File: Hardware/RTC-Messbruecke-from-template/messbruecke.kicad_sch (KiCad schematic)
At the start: 24 parts, among them U3 MAX6105, U4 LM324

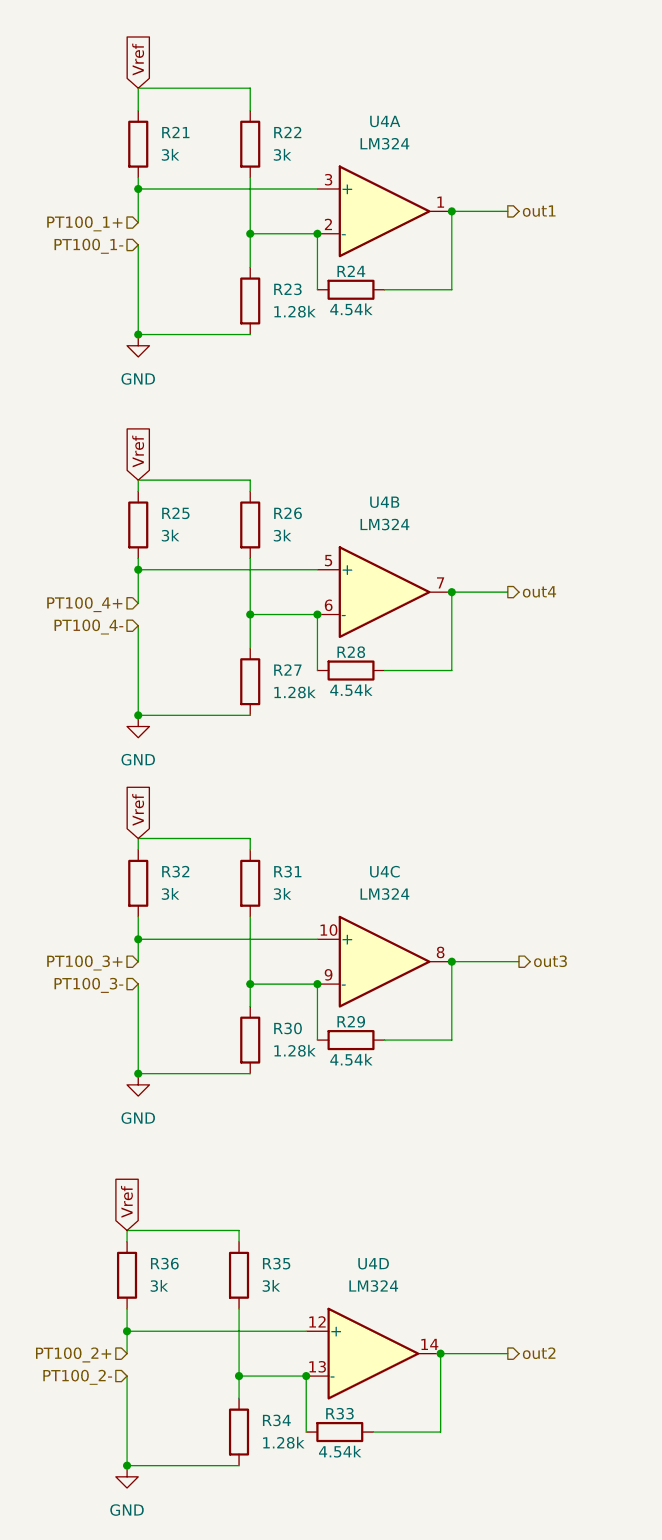
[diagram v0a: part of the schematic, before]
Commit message: added picture of schematic
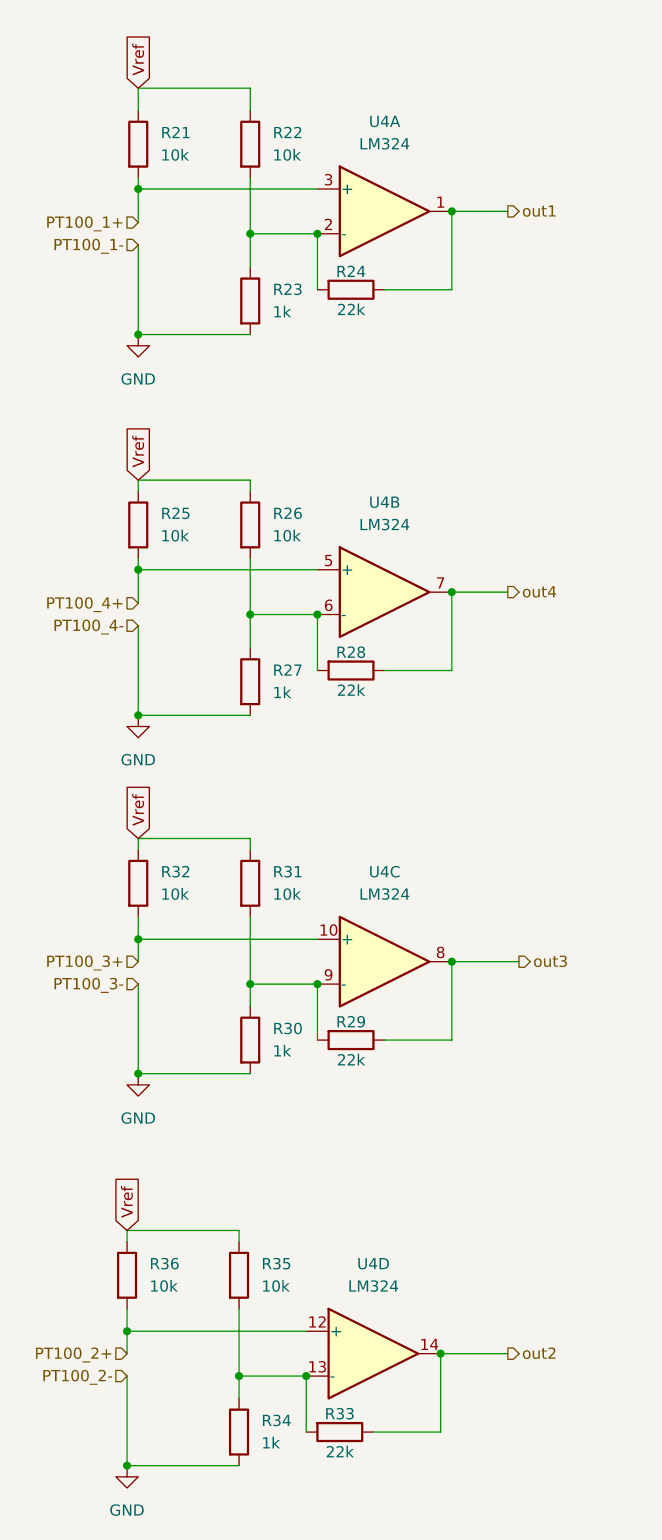
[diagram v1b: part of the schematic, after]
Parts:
- R21, R22, R25, R26, R31, R32, R35, R36: value 3k -> 10k
- R23, R27, R30, R34: value 1.28k -> 1k
- R24, R28, R29, R33: value 4.54k -> 22k
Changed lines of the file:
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@@
 			)
 		)
-		(property "Value" "3k"
+		(property "Value" "10k"
 			(at 50.8 161.2899 0)
 			(effects
@@
 			)
 		)
-		(property "Value" "1.28k"
+		(property "Value" "1k"
 			(at 52.07 134.6199 0)
 			(effects
@@
 			)
 		)
-		(property "Value" "1.28k"
+		(property "Value" "1k"
 			(at 52.07 50.7999 0)
 			(effects
@@
 			)
 		)
-		(property "Value" "4.54k"
+		(property "Value" "22k"
 			(at 59.69 180.086 90)
 			(effects
@@
 			)
 		)
-		(property "Value" "4.54k"
+		(property "Value" "22k"
 			(at 60.96 135.636 90)
 			(effects
@@
 			)
 		)
-		(property "Value" "3k"
+		(property "Value" "10k"
 			(at 38.1 161.2899 0)
 			(effects
@@
 			)
 		)
-		(property "Value" "1.28k"
+		(property "Value" "1k"
 			(at 50.8 179.0699 0)
 			(effects
@@
 			)
 		)
-		(property "Value" "3k"
+		(property "Value" "10k"
 			(at 52.07 33.0199 0)
 			(effects
@@
 			)
 		)
-		(property "Value" "3k"
+		(property "Value" "10k"
 			(at 39.37 33.0199 0)
 			(effects
@@
 			)
 		)
-		(property "Value" "1.28k"
+		(property "Value" "1k"
 			(at 52.07 93.9799 0)
 			(effects
@@
 			)
 		)
-		(property "Value" "3k"
+		(property "Value" "10k"
 			(at 52.07 116.8399 0)
 			(effects
@@
 			)
 		)
-		(property "Value" "4.54k"
+		(property "Value" "22k"
 			(at 60.96 93.726 90)
 			(effects
@@
 			)
 		)
-		(property "Value" "3k"
+		(property "Value" "10k"
 			(at 39.37 116.8399 0)
 			(effects
@@
 			)
 		)
-		(property "Value" "3k"
+		(property "Value" "10k"
 			(at 39.37 76.1999 0)
 			(effects
@@
 			)
 		)
-		(property "Value" "4.54k"
+		(property "Value" "22k"
 			(at 60.96 50.546 90)
 			(effects
@@
 			)
 		)
-		(property "Value" "3k"
+		(property "Value" "10k"
 			(at 52.07 76.1999 0)
 			(effects

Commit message: modified readme
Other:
- company: (none) -> LMWB
- title: Template Arduino Shield Simple Outline -> 4-Fach Messbruecke PT1000
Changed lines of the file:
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@@
 	(paper "A4")
 	(title_block
-		(title "Template Arduino Shield Simple Outline")
-		(date "2024-08-05")
+		(title "4-Fach Messbruecke PT1000")
+		(date "2024-09-02")
 		(rev "v.0.2")
+		(company "LMWB")
+		(comment 1 "Lukas Bartels 2024")
 	)
 	(junction

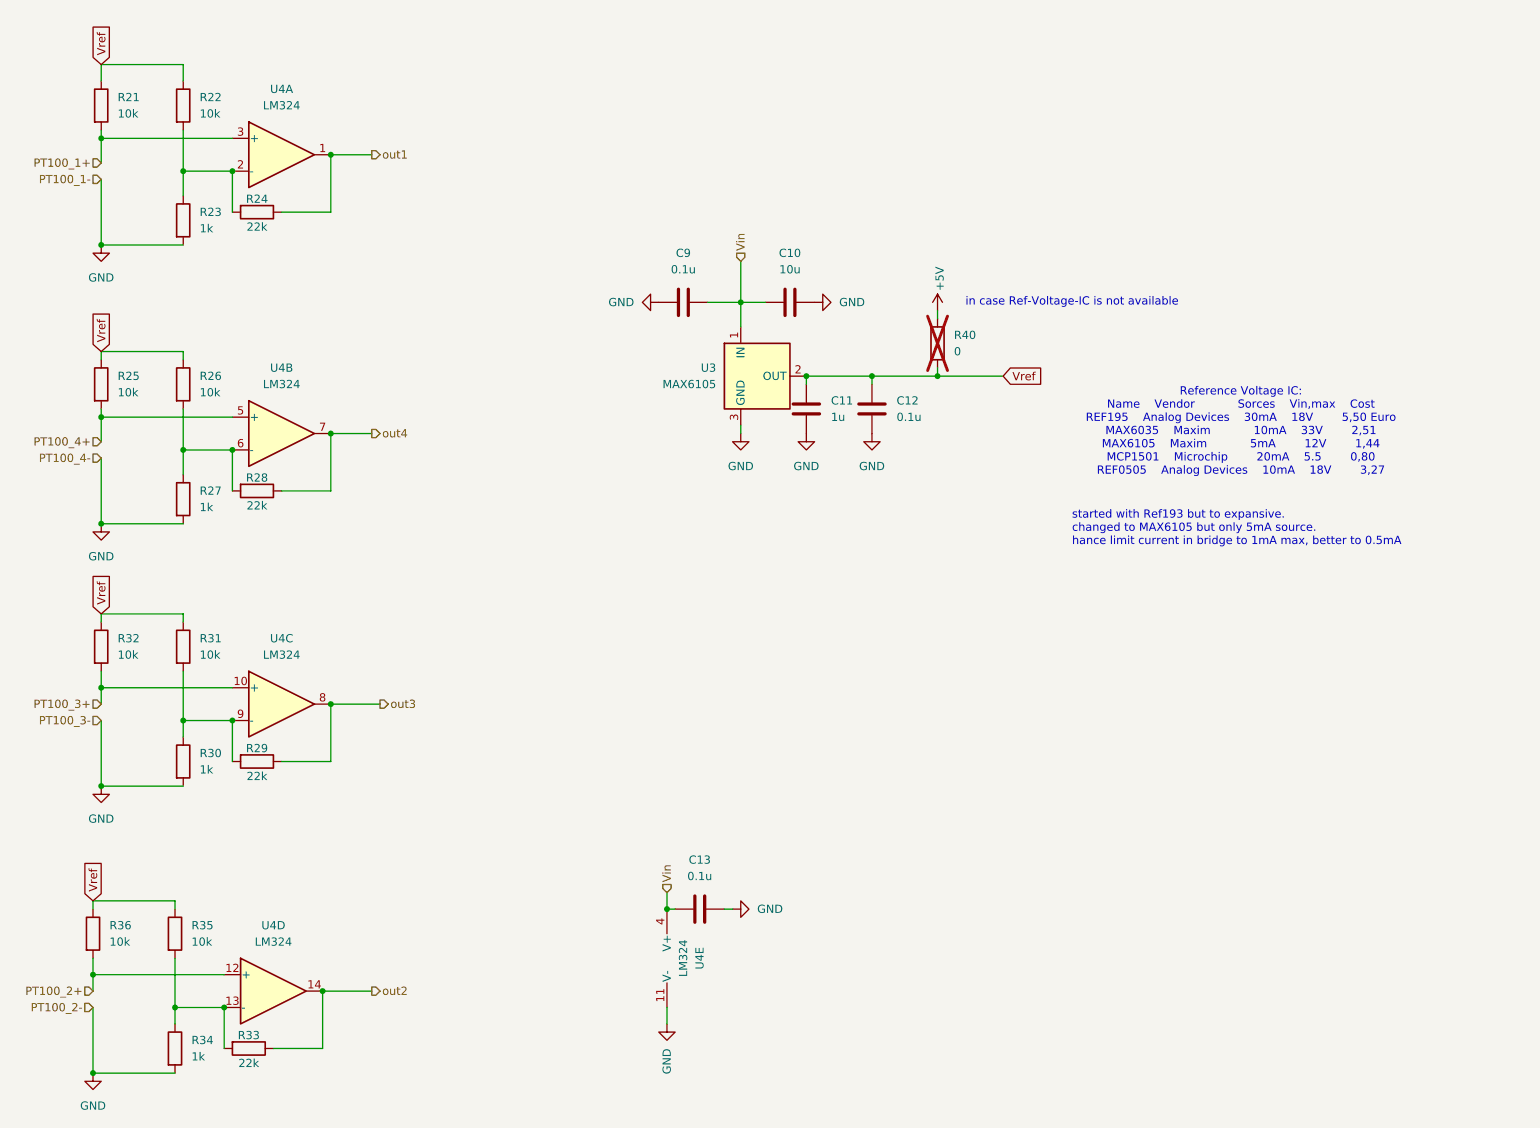
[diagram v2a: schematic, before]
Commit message: added test results and simulations
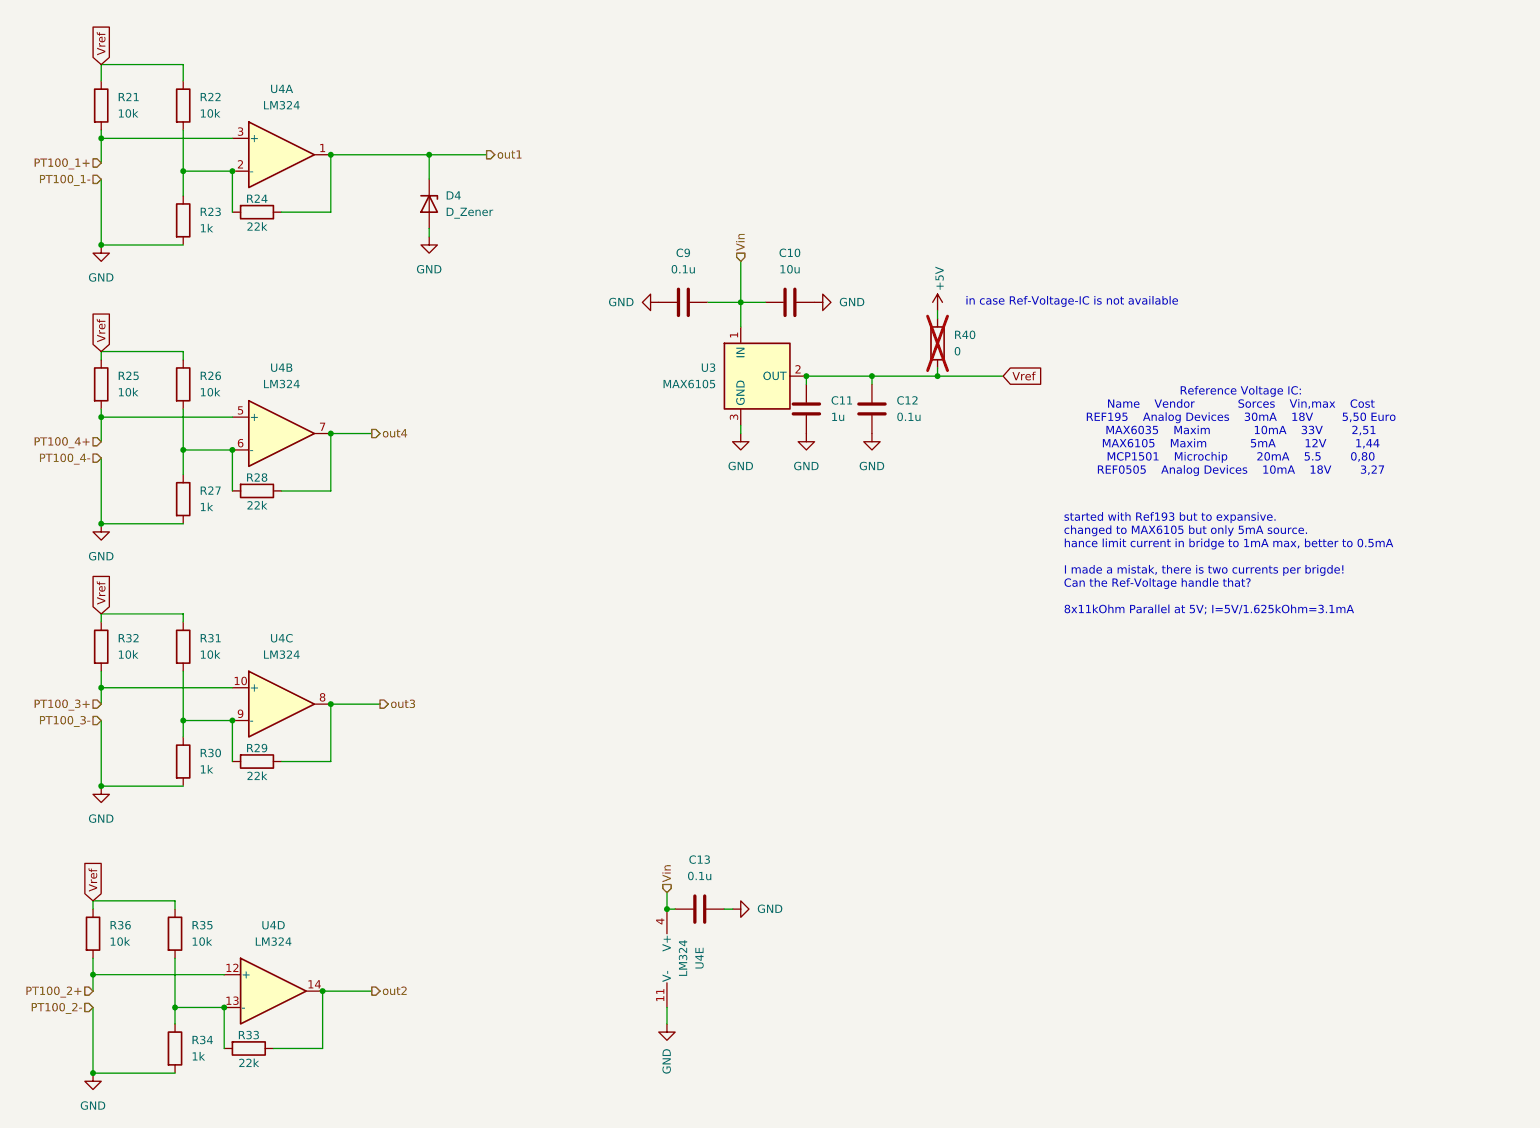
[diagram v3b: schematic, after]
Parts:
- added D4: D_Zener, Diode_SMD:D_1206_3216Metric, symbol Device:D_Zener
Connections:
- net GND: now also D4.2 (A)
- net out1: now also D4.1 (K)
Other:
- note added: "started with Ref193 but to expansive. changed to MAX6105 but only 5mA source. hance limit current in bridge to 1mA max, better to 0.5mA I made a mistak, there is two currents per brigde! Can the Ref-Voltage handle that? 8x11kOhm Parallel at 5V; I=5V/1.625kOhm=3.1mA"
- note removed: "started with Ref193 but to expansive. changed to MAX6105 but only 5mA source. hance limit current in bridge to 1mA max, better to 0.5mA"
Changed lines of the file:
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@@
+	)
+	(junction
+		(at 87.63 39.37)
+		(diameter 0)
+		(color 0 0 0 0)
 	)
 	(junction
@@
 	(wire
 		(pts
+			(xy 87.63 39.37) (xy 96.52 39.37)
+		)
+		(stroke
+			(width 0)
+			(type default)
+		)
+	)
+	(wire
+		(pts
 			(xy 146.05 73.66) (xy 146.05 74.93)
 		)
@@
 	(wire
 		(pts
+			(xy 87.63 50.8) (xy 87.63 52.07)
+		)
+		(stroke
+			(width 0)
+			(type default)
+		)
+	)
+	(wire
+		(pts
 			(xy 72.39 48.26) (xy 72.39 39.37)
 		)
@@
 	(wire
 		(pts
-			(xy 72.39 39.37) (xy 78.74 39.37)
+			(xy 72.39 39.37) (xy 87.63 39.37)
 		)
 		(stroke
@@
 		(pts
 			(xy 36.83 127) (xy 36.83 137.16)
+		)
+		(stroke
+			(width 0)
+			(type default)
+		)
+	)
+	(wire
+		(pts
+			(xy 87.63 39.37) (xy 87.63 43.18)
 		)
 		(stroke
@@
 		)
 	)
-	(text "started with Ref193 but to expansive.\nchanged to MAX6105 but only 5mA source.\nhance limit current in bridge to 1mA max, better to 0.5mA "
+	(text "started with Ref193 but to expansive.\nchanged to MAX6105 but only 5mA source.\nhance limit current in bridge to 1mA max, better to 0.5mA\n\nI made a mistak, there is two currents per brigde!\nCan the Ref-Voltage handle that?\n\n8x11kOhm Parallel at 5V; I=5V/1.625kOhm=3.1mA"
 		(exclude_from_sim no)
-		(at 187.198 97.282 0)
+		(at 185.928 102.87 0)
 		(effects
 			(font
@@
 	(hierarchical_label "out1"
 		(shape output)
-		(at 78.74 39.37 0)
+		(at 96.52 39.37 0)
 		(fields_autoplaced yes)
 		(effects
@@
 			)
 			(justify left)
+		)
+	)
+	(symbol
+		(lib_id "Library:GND")
+		(at 87.63 52.07 0)
+		(unit 1)
+		(exclude_from_sim no)
+		(in_bom yes)
+		(on_board yes)
+		(dnp no)
+		(fields_autoplaced yes)
+		(property "Reference" "#PWR07"
+			(at 87.63 58.42 0)
+			(effects
+				(font
+					(size 1.27 1.27)
+				)
+				(hide yes)
+			)
+		)
+		(property "Value" "GND"
+			(at 87.63 57.15 0)
+			(effects
+				(font
+					(size 1.27 1.27)
+				)
+			)
+		)
+		(property "Footprint" ""
+			(at 87.63 52.07 0)
+			(effects
+				(font
+					(size 1.27 1.27)
+				)
+				(hide yes)
+			)
+		)
+		(property "Datasheet" ""
+			(at 87.63 52.07 0)
+			(effects
+				(font
+					(size 1.27 1.27)
+				)
+				(hide yes)
+			)
+		)
+		(property "Description" "Power symbol creates a global label with name \"GND\" , ground"
+			(at 87.63 52.07 0)
+			(effects
+				(font
+					(size 1.27 1.27)
+				)
+				(hide yes)
+			)
+		)
+		(pin "1"
+		)
+		(instances
+			(project "RTC-Messbruecke-from-template"
+				(path "/e63e39d7-6ac0-4ffd-8aa3-1841a4541b55/85f37e4c-ec8b-4781-8436-42b879b587e6"
+					(reference "#PWR07")
+					(unit 1)
+				)
+			)
 		)
 	)
@@
 					(unit 1)
 				)
+			)
+		)
+	)
+	(symbol
+		(lib_id "Device:D_Zener")
+		(at 87.63 46.99 270)
+		(unit 1)
+		(exclude_from_sim no)
+		(in_bom yes)
+		(on_board yes)
+		(dnp no)
+		(fields_autoplaced yes)
+		(property "Reference" "D4"
+			(at 90.17 45.7199 90)
+			(effects
+				(font
+					(size 1.27 1.27)
+				)
+				(justify left)
+			)
+		)
+		(property "Value" "D_Zener"
+			(at 90.17 48.2599 90)
+			(effects
+				(font
+					(size 1.27 1.27)
+				)
+				(justify left)
+			)
+		)
+		(property "Footprint" "Diode_SMD:D_1206_3216Metric"
+			(at 87.63 46.99 0)
+			(effects
+				(font
+					(size 1.27 1.27)
+				)
+				(hide yes)
+			)
+		)
+		(property "Datasheet" "~"
+			(at 87.63 46.99 0)
+			(effects
+				(font
+					(size 1.27 1.27)
+				)
+				(hide yes)
+			)
+		)
+		(property "Description" "Zener diode"
+			(at 87.63 46.99 0)
+			(effects
+				(font
+					(size 1.27 1.27)
+				)
+				(hide yes)
+			)
+		)
+		(pin "2"
+		)
+		(pin "1"
+		)
+		(instances
+			(project ""
+				(path "/e63e39d7-6ac0-4ffd-8aa3-1841a4541b55/85f37e4c-ec8b-4781-8436-42b879b587e6"
+					(reference "D4")
+					(unit 1)
+				)

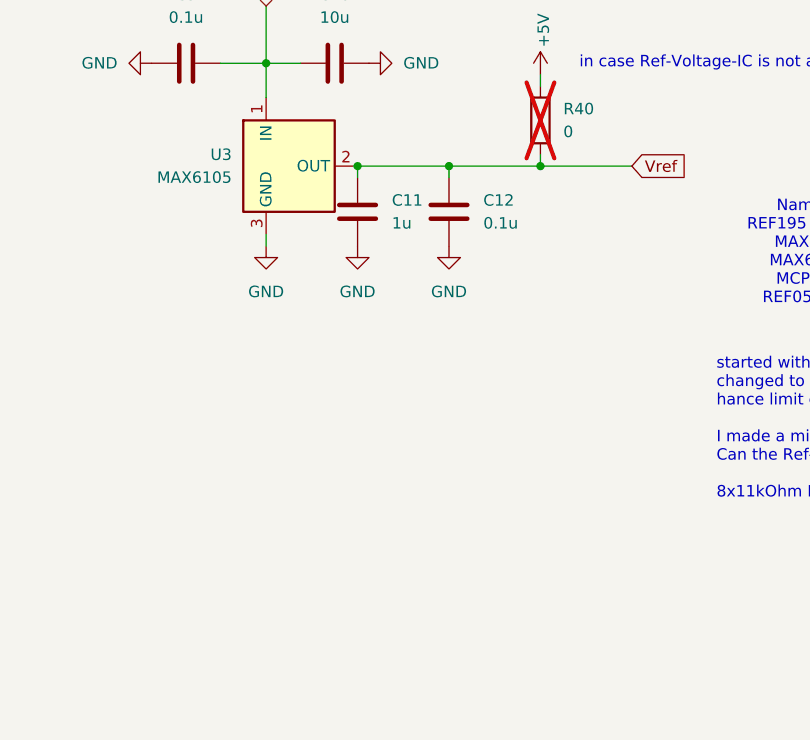
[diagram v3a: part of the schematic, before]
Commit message: added REF-195 as alternativ voltage reference
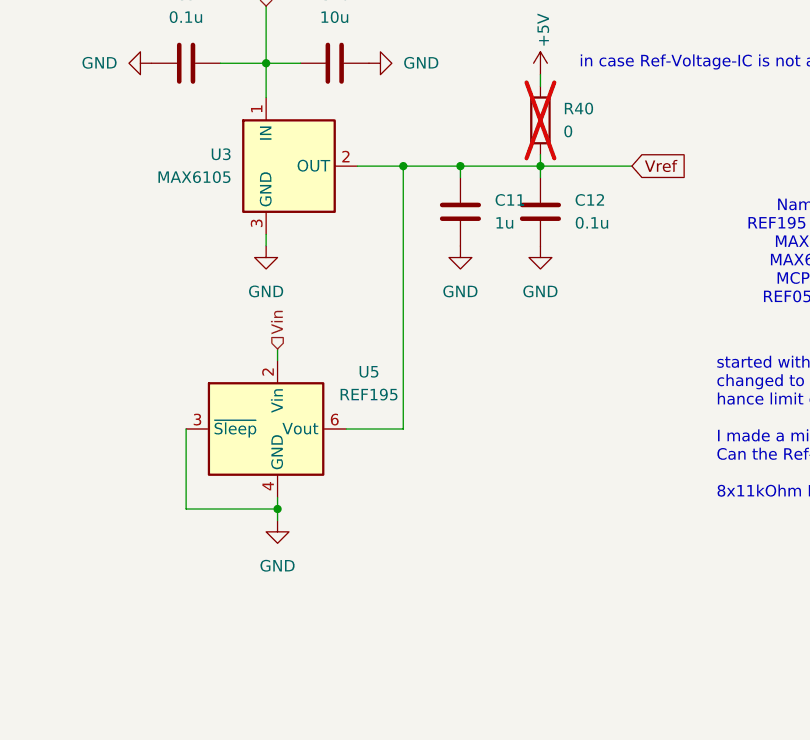
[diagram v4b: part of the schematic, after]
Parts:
- added U5: REF195, Package_SO:SOIC-8_3.9x4.9mm_P1.27mm, symbol Reference_Voltage:REF195
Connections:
- net GND: now also U5.3 (~{Sleep}), U5.4 (GND)
- net Vin: now also U5.2 (Vin)
- net Vref: now also U5.6 (Vout)
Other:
- moved on the sheet: C11, C12
